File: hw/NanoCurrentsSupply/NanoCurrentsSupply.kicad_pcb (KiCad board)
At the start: 2 copper layers, 40.8 x 43.2 mm, 49 parts, among them J1 Conn_01x05_Pin, J2 Screw_Terminal_01x02, J3 Conn_02x03_Counter_Clockwise, J4 Conn_Coaxial, J5 Conn_Coaxial, U1 ADS1015IDGS, U2 INA240A1D, U3 LP2980-ADJ, U4 LP2980-ADJ, U5 LP2980-ADJ, U6 LP2980-ADJ, U7 LMV358

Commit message: Finished first PCB of NanoCurrentsSupply
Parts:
- Rs1: value R -> 1; footprint Resistor_SMD:R_4020_10251Metric_Pad1.65x5.30mm_HandSolder -> Resistor_SMD:R_1206_3216Metric_Pad1.30x1.75mm_HandSolder
- moved C8 31.8 mm to (124.8, 23.2), turned to 0 degrees
- moved C3 31.6 mm to (99.9, 34.0), turned to 180 degrees
- moved R4 30.7 mm to (96.1, 30.0), turned to 180 degrees
- moved R3 29.2 mm to (99.9, 32.0), turned to 180 degrees
- moved C10 27.6 mm to (126.6, 30.0), turned to 0 degrees
- moved R5 27.0 mm to (99.9, 30.0), turned to 180 degrees
- moved U5 26.5 mm to (122.8, 26.5), turned to -90 degrees
- moved C4 24.0 mm to (103.6, 30.0), turned to 0 degrees
- moved U3 23.6 mm to (99.8, 26.6), turned to -90 degrees
- moved R11 23.2 mm to (122.8, 30.0), turned to 180 degrees
- moved R9 21.7 mm to (122.8, 31.8), turned to 180 degrees
- moved C9 20.4 mm to (122.8, 33.5), turned to 180 degrees
- moved R10 19.3 mm to (119.0, 30.0), turned to 180 degrees
- moved C2 18.3 mm to (101.9, 23.3), turned to 0 degrees
- moved C12 10.6 mm to (117.5, 46.2), turned to 180 degrees
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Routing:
- net VCC: track 0.00 -> 73.0 mm
- net GND: track 0.00 -> 56.8 mm, vias 0 -> 102
- net +5VP: track 0.00 -> 46.2 mm, vias 0 -> 2
- net +1V8: track 0.00 -> 31.4 mm
- net RS_LOW: track 0.00 -> 28.8 mm
- net +3.3V: track 0.00 -> 20.3 mm
- net ADC_RDY: track 0.00 -> 18.0 mm
- net I2C_SCL: track 0.00 -> 13.9 mm
- net +5V: track 0.00 -> 13.6 mm
- net I2C_SDA: track 0.00 -> 13.2 mm
- net Net-(U7A--): track 0.00 -> 9.73 mm
- net Net-(U3-ADJ): track 0.00 -> 8.24 mm
- net Net-(U4-ADJ): track 0.00 -> 8.07 mm
- net Net-(U6-ADJ): track 0.00 -> 7.98 mm
- net Net-(U5-ADJ): track 0.00 -> 7.82 mm
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- added copper zone on B.Cu, net GND
- added copper zone on F.Cu, net GND
- added copper zone on F.Cu, net RS_HIGH
- added copper zone on F.Cu, net RS_LOW
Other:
- board text added: "ADC_RDY"
- board text added: "GND"
- board text added: "NanoCurrentsSupply AP 2025"
- board text added: "SCL"
- board text added: "SDA"
- board text added: "SHUNT_HIGH"
- board text added: "SHUNT_LOW"
- board text added: "VCC"
- board text added: "V_DUT"

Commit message: Update HW before production
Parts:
- added D1: LED, LED_SMD:LED_0603_1608Metric, F.Cu at (124.8, 40.4)
- added R19: 200, Resistor_SMD:R_0603_1608Metric_Pad0.98x0.95mm_HandSolder, F.Cu at (121.2, 40.4)
- R15, R16: value ~ -> 0
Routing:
- net Net-(D1-A): track 0.00 -> 1.90 mm
- net +5VP: track 46.2 -> 48.1 mm
- net GND: track 56.8 -> 58.0 mm, vias 102 -> 91

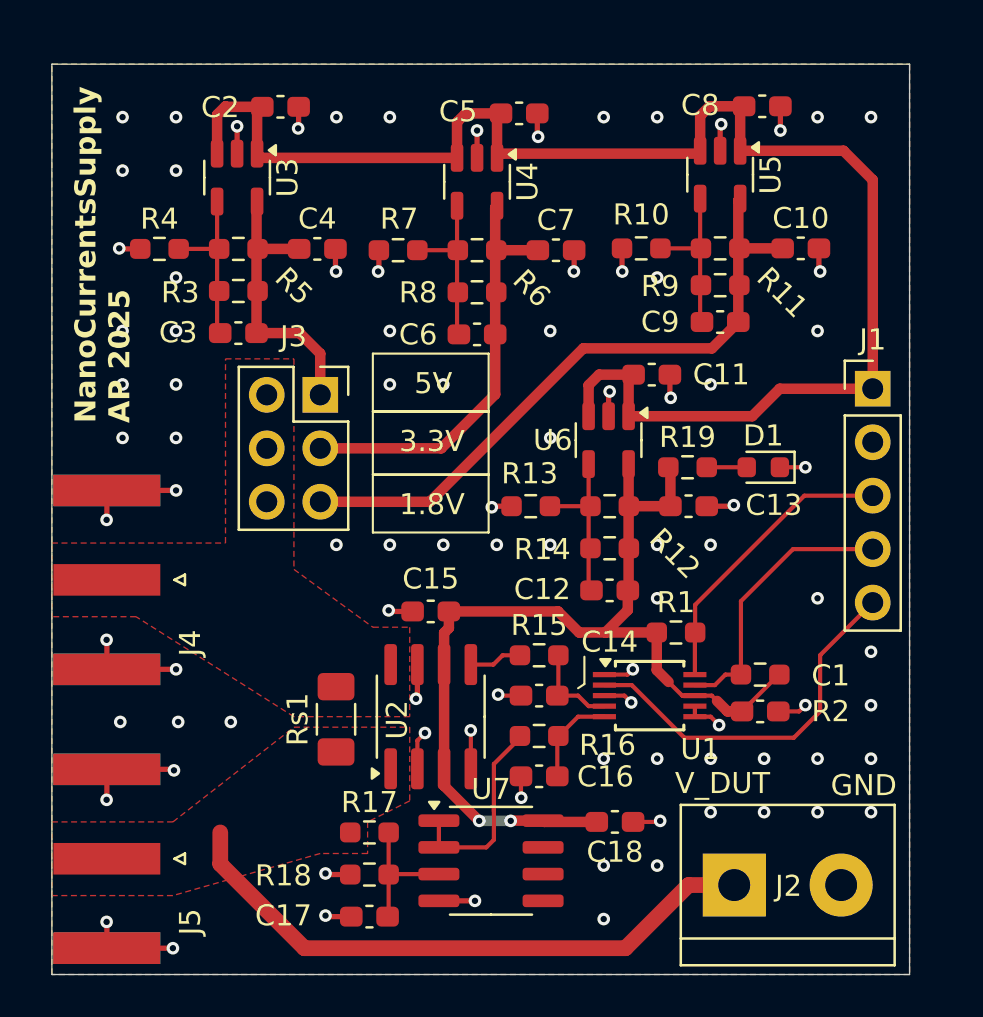
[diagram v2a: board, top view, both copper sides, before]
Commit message: Rev B00 : only use one regulator
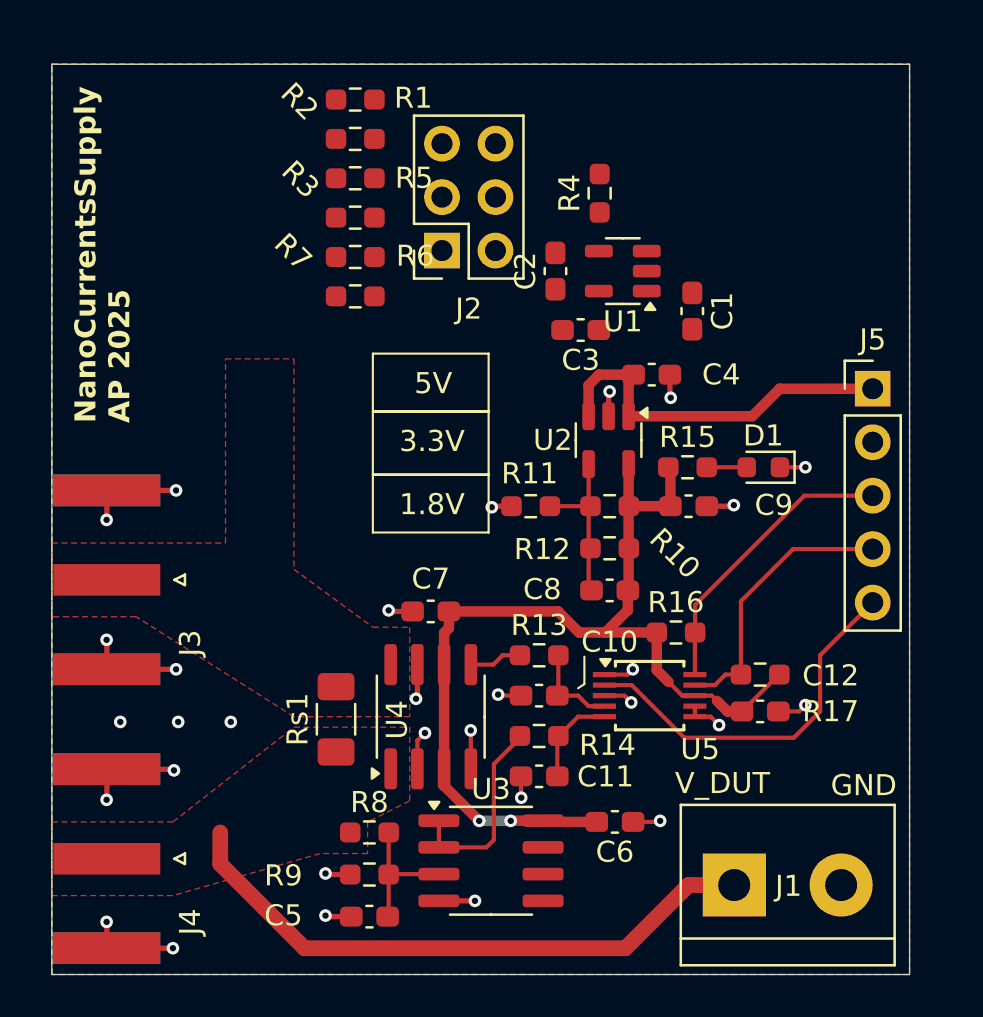
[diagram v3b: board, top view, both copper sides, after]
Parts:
- removed the C10 at (126.6, 30.0)
- removed the C4 at (103.6, 30.0)
- removed the C5 at (113.2, 23.6)
- removed the C6 at (111.2, 34.1)
- removed the C7 at (115.0, 30.1)
- removed the C8 at (124.8, 23.2)
- removed the C9 at (122.8, 33.5)
- removed the J3 at (103.8, 37.0)
- removed the R10 at (119.0, 30.0)
- removed the R7 at (107.5, 30.1)
- removed the U3 at (99.8, 26.6)
- removed the U4 at (111.2, 26.8)
- removed the U5 at (122.8, 26.5)
- added C1: 1uF, Capacitor_SMD:C_0603_1608Metric_Pad1.08x0.95mm_HandSolder, F.Cu at (121.4, 33.0)
- added J2: Conn_02x03_Counter_Clockwise, Connector_PinSocket_2.54mm:PinSocket_2x03_P2.54mm_Vertical, F.Cu at (109.5, 30.1)
- added U1: LP2980-ADJ, Package_TO_SOT_SMD:SOT-23-5, F.Cu at (118.1, 31.1)
- C2: value 1uF -> 0.1uF
- C3: value 0.1uF -> 4.7uF
- moved R4 21.1 mm to (117.0, 27.4), turned to 90 degrees
- moved R7 17.5 mm to (105.4, 32.3), turned to 0 degrees
- moved R6 17.4 mm to (105.4, 30.4), turned to 0 degrees
- moved C3 16.3 mm to (116.1, 33.9)
- moved C2 15.2 mm to (114.9, 31.1), turned to 90 degrees
- moved R1 10.7 mm to (105.4, 22.9), turned to 0 degrees
- moved R5 7.93 mm to (105.4, 26.7), turned to 0 degrees
- moved R2 7.62 mm to (105.4, 24.8), turned to 0 degrees
- moved R3 5.99 mm to (105.4, 28.5), turned to 0 degrees
- renumbered C14 to C10, C16 to C11, C1 to C12, C11 to C4, C17 to C5, C18 to C6, C15 to C7, C12 to C8, C13 to C9, J2 to J1, J4 to J3, J5 to J4, J1 to J5, R3 to R1, R12 to R10, R13 to R11, R14 to R12, R15 to R13, R16 to R14, R19 to R15, R1 to R16, R2 to R17, R5 to R2, R6 to R3, R8 to R5, R9 to R6, R11 to R7, R17 to R8, R18 to R9, U6 to U2, U7 to U3, U2 to U4, U1 to U5
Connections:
- C2 pad 1: VCC -> RS_HIGH
- C2 pad 2: GND -> /FB_DIVIDER_OUT
- C3 pad 1: +5V -> RS_HIGH
- C3 pad 2: Net-(U3-ADJ) -> GND
- R1 pad 1: +5V -> RS_HIGH
- R1 pad 2: Net-(U3-ADJ) -> Net-(J2-Pin_5)
- R2 pad 1: +5V -> RS_HIGH
- R2 pad 2: Net-(U3-ADJ) -> Net-(J2-Pin_5)
- R3 pad 1: +3.3V -> RS_HIGH
- R4 pad 1: Net-(U3-ADJ) -> /FB_DIVIDER_OUT
- R5 pad 1: +3.3V -> RS_HIGH
- R6 pad 1: +1V8 -> RS_HIGH
- R7 pad 1: +1V8 -> RS_HIGH
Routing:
- net VCC: track 73.0 -> 18.0 mm
- net +1V8: track 31.4 -> 0.00 mm
- net +3.3V: track 20.3 -> 0.00 mm
- net +5V: track 13.6 -> 0.00 mm
- net GND: track 58.0 -> 44.5 mm, vias 91 -> 30
- net Net-(U3-ADJ): track 8.24 -> 0.00 mm
- net Net-(J2-Pin_3): track 8.07 -> 0.00 mm
- net Net-(J2-Pin_1): track 7.82 -> 0.00 mm
